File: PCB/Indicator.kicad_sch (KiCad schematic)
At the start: 6 parts

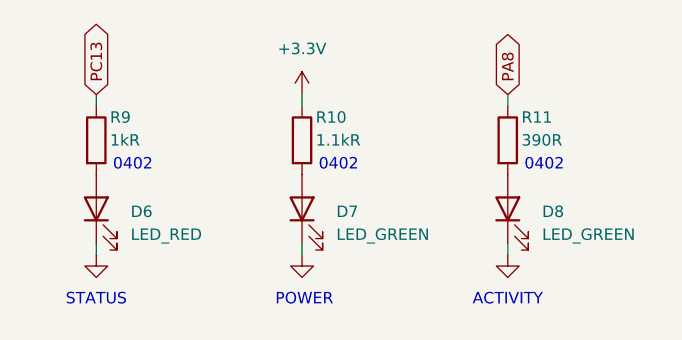
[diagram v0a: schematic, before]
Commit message: Improved Protection and Board Testability - Added power rail protection and decoupling for stepper motor noise environment - Added TVS, bulk caps and fuse upgrade on 24V rail - Added test pads for bring-up and debugging
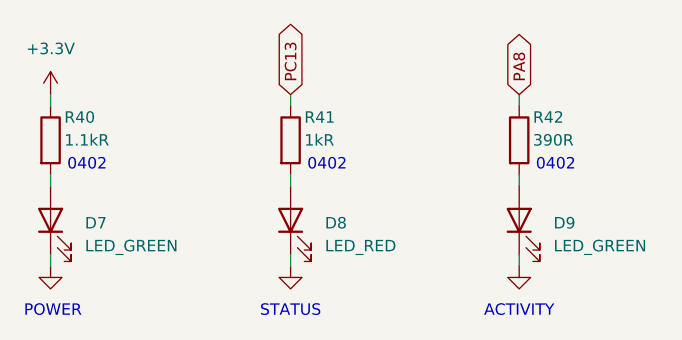
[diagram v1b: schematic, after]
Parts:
- renumbered D6 to D8, D8 to D9, R10 to R40, R9 to R41, R11 to R42
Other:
- moved on the sheet: D7, D8, D9, R40, R41, R42

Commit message: PCB Layout: Initial TMC2209 driver cluster layout
- Defined netclasses for 24V, Stepper Motor, 3V3, 5V and Signal
- Decided on 4-layer stackup: Signal / GND / Power / Signal
- Routed high current motor output traces with tapered zone fills
- Placed and routed VS decoupling caps (100nF, 1uF, 47uF electrolytic)
- Routed sense resistors with dedicated GND vias per resistor
- Routed BRA/BRB via bottom layer with perpendicular crossing under motor traces
- Planned +24V / +3V3 split power plane on L3
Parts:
- D9: value LED_GREEN -> LED_BLUE
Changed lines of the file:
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@@
 			)
 		)
-		(property "Value" "LED_GREEN"
+		(property "Value" "LED_BLUE"
 			(at 78.74 43.4974 90)
 			(show_name no)

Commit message: Started laying out the PCB - Decided for a square-shaped board - Split Motor Controllers on top and bottom - Split Power Plane (+3V3 on logic side, +24V on motor side) - Roughly layed out the board entirely - Reconsidered my life choises (got sick)
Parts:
- renumbered R40 to R10, R41 to R11, R42 to R12
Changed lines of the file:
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@@
 		(dnp no)
 		(fields_autoplaced yes)
-		(property "Reference" "#PWR0174"
+		(property "Reference" "#PWR042"
 			(at 22.86 52.07 0)
 			(hide yes)
@@
 			(project "Arm_Controller"
 				(path "/2323d903-32ae-4da3-a89f-487023e10892/b95fa2d1-f2ed-401b-b984-3832c1794be1"
-					(reference "#PWR0174")
+					(reference "#PWR042")
 					(unit 1)
 				)
@@
 		(dnp no)
 		(fields_autoplaced yes)
-		(property "Reference" "#PWR0175"
+		(property "Reference" "#PWR043"
 			(at 49.53 52.07 0)
 			(hide yes)
@@
 			(project "Arm_Controller"
 				(path "/2323d903-32ae-4da3-a89f-487023e10892/b95fa2d1-f2ed-401b-b984-3832c1794be1"
-					(reference "#PWR0175")
+					(reference "#PWR043")
 					(unit 1)
 				)
@@
 		(in_pos_files yes)
 		(dnp no)
-		(property "Reference" "R41"
+		(property "Reference" "R11"
 			(at 51.054 29.21 0)
 			(show_name no)
@@
 			(project "Arm_Controller"
 				(path "/2323d903-32ae-4da3-a89f-487023e10892/b95fa2d1-f2ed-401b-b984-3832c1794be1"
-					(reference "R41")
+					(reference "R11")
 					(unit 1)
 				)
@@
 		(in_pos_files yes)
 		(dnp no)
-		(property "Reference" "R42"
+		(property "Reference" "R12"
 			(at 76.454 29.21 0)
 			(show_name no)
@@
 			(project "Arm_Controller"
 				(path "/2323d903-32ae-4da3-a89f-487023e10892/b95fa2d1-f2ed-401b-b984-3832c1794be1"
-					(reference "R42")
+					(reference "R12")
 					(unit 1)
 				)
@@
 		(dnp no)
 		(fields_autoplaced yes)
-		(property "Reference" "#PWR0173"
+		(property "Reference" "#PWR041"
 			(at 22.86 30.48 0)
 			(hide yes)
@@
 			(project "Arm_Controller"
 				(path "/2323d903-32ae-4da3-a89f-487023e10892/b95fa2d1-f2ed-401b-b984-3832c1794be1"
-					(reference "#PWR0173")
+					(reference "#PWR041")
 					(unit 1)
 				)
@@
 		(in_pos_files yes)
 		(dnp no)
-		(property "Reference" "R40"
+		(property "Reference" "R10"
 			(at 24.384 29.21 0)
 			(show_name no)
@@
 			(project "Arm_Controller"
 				(path "/2323d903-32ae-4da3-a89f-487023e10892/b95fa2d1-f2ed-401b-b984-3832c1794be1"
-					(reference "R40")
+					(reference "R10")
 					(unit 1)
 				)
@@
 		(dnp no)
 		(fields_autoplaced yes)
-		(property "Reference" "#PWR0176"
+		(property "Reference" "#PWR044"
 			(at 74.93 52.07 0)
 			(hide yes)
@@
 			(project "Arm_Controller"
 				(path "/2323d903-32ae-4da3-a89f-487023e10892/b95fa2d1-f2ed-401b-b984-3832c1794be1"
-					(reference "#PWR0176")
-					(unit 1)
-				)
+					(reference "#PWR044")
+					(unit 1)
+				)
